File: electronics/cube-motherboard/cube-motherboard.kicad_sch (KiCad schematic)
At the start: 52 parts, among them J1 Conn_01x02, J2 Conn_02x04_Top_Bottom, J3 Conn_02x04_Top_Bottom, J4 Conn_02x04_Top_Bottom, J5 Conn_01x18, Q1 BSS138, Q2 BSS138, U1 Escon_24/2, U2 Escon_24/2, U3 Escon_24/2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

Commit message: Organize esp32 <-> escon wiring
Remapped AO1 of M3 to an ADC1 pin.
Removed all three unused AO2 DI3 wirings and relevant diodes and capacitors
Corrected pins.h (Old version was not matching with old schematic btw)
Updated Bom accordingly
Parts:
- removed C11, C7, C9: 0.1uF, Capacitor_SMD:C_0603_1608Metric, symbol Device:C
- removed D10, D6, D8: D_TVS, Diode_SMD:D_0402_1005Metric, symbol Device:D_TVS
- C11: renamed from C16; symbol Device:C_Polarized -> Device:C
- renumbered C15 to C10, C8 to C7, C10 to C8, C14 to C9, D7 to D6, D9 to D7
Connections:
- net AO1_M3: now also U4.7 (GPIO7/ADC1_CH6); no longer U4.8 (GPIO15/ADC2_CH4/32K_P)
- net AO2_M1: no longer names the net of U1.19 (AO2)
- net AO2_M1: no longer U4.17 (GPIO11/ADC2_CH0)
- net AO2_M2: no longer names the net of U4.12 (GPIO8/ADC1_CH7)
- net AO2_M2: no longer U2.19 (AO2)
- net AO2_M3: no longer names the net of U3.19 (AO2)
- net AO2_M3: no longer U4.7 (GPIO7/ADC1_CH6)
- net DI3_M1: no longer names the net of U1.15 (DIO3)
- net DI3_M1: no longer U4.20 (GPIO14/ADC2_CH3)
- net DI3_M2: no longer names the net of U4.9 (GPIO16/ADC2_CH5/32K_N)
- net DI3_M2: no longer U2.15 (DIO3)
- net DI3_M3: no longer names the net of U3.15 (DIO3)
- net DI3_M3: no longer U4.4 (GPIO4/ADC1_CH3)
- no-connect marks 46 -> 59
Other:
- moved on the sheet: C7, C8, D5, D6, D7

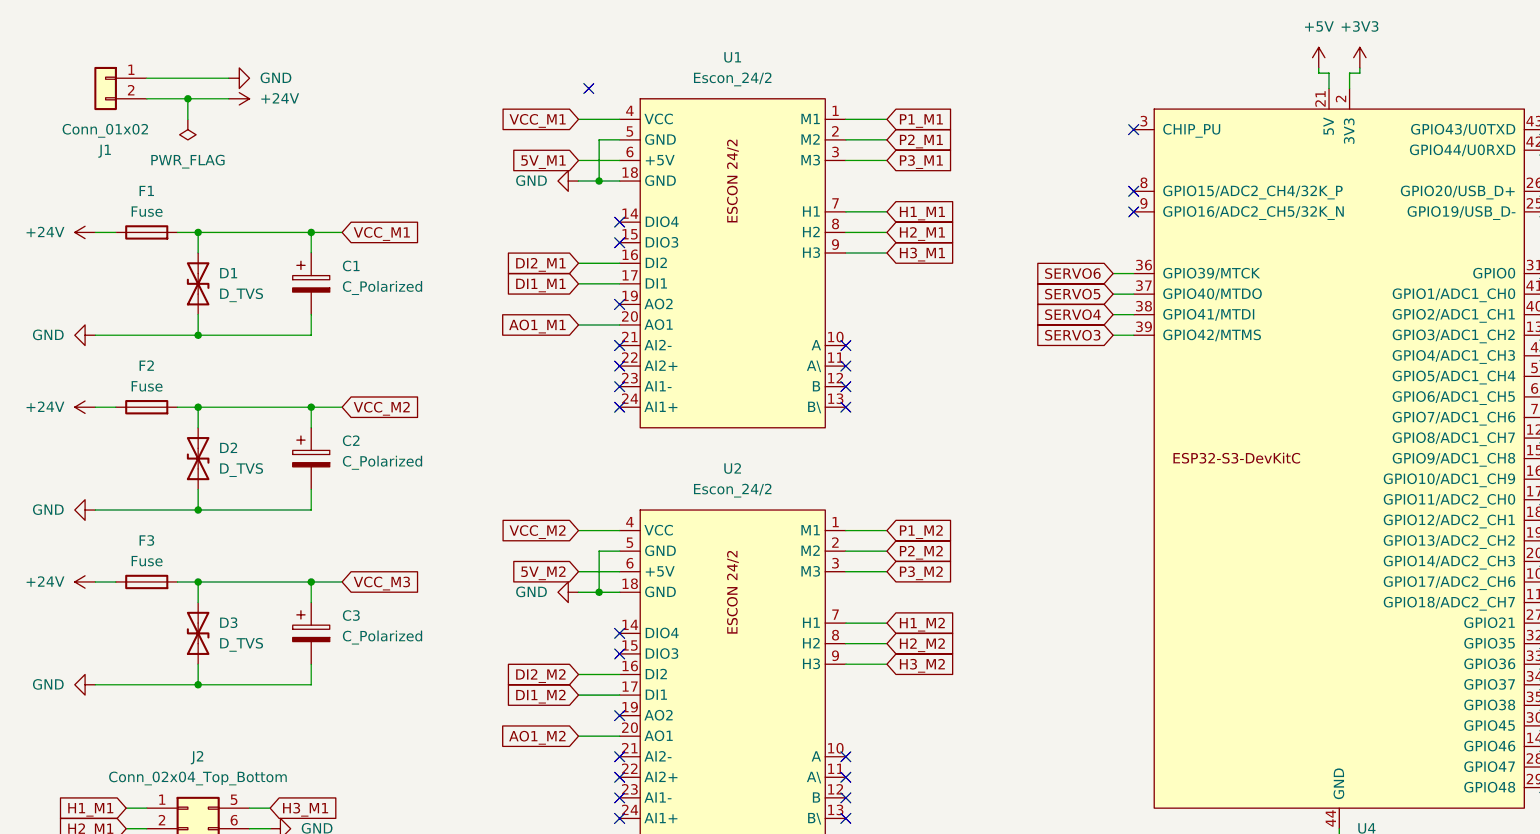
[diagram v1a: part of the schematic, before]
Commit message: Fix symbol, footprint and orientation of D1,D2 and D3 diodes
Add missing 3D models for L1 & F1,F2,F3
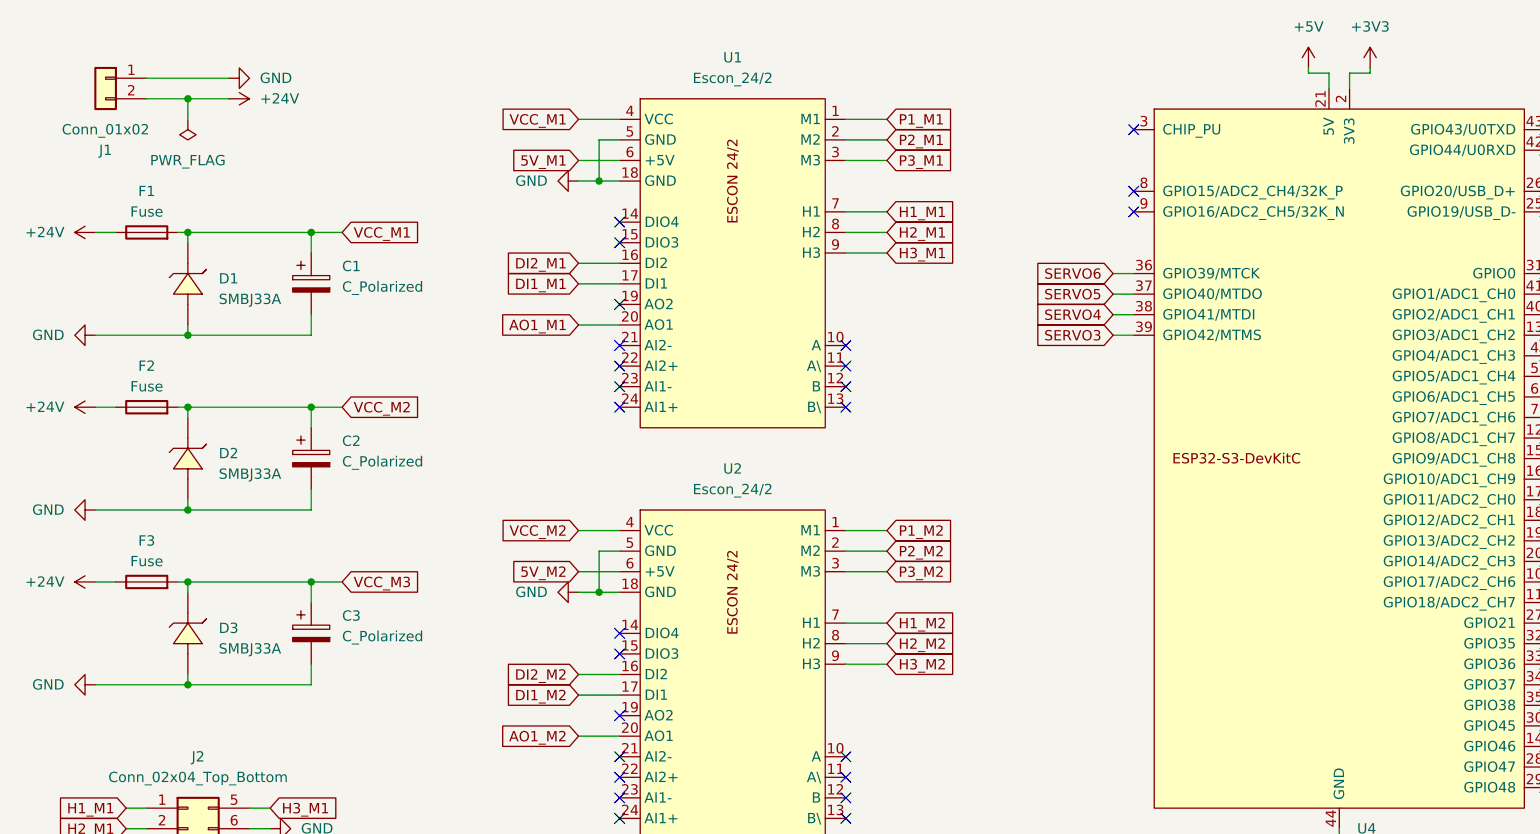
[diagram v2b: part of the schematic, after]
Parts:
- removed D1, D2, D3: D_TVS, Diode_SMD:D_SMB, symbol Device:D_TVS
- added D1, D2, D3: SMBJ33A, cube-motherboard:SMB_L4.4-W3.6-LS5.4-RD, symbol cube-motherboard:SMBJ33A
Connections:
- net GND: now also D1.2 (A), D2.2 (A), D3.2 (A)
- net VCC_M1: now also D1.1 (C)
- net VCC_M2: now also D2.1 (C)
- net VCC_M3: now also D3.1 (C)
- no-connect marks 59 -> 58

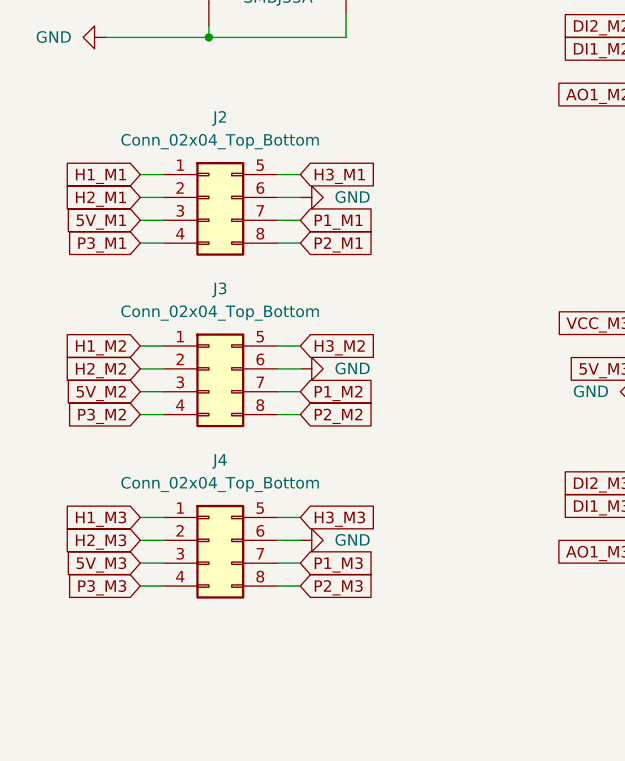
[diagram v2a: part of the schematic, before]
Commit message: Remove the requirement to remap the pins of the molex cables by reorganizing pin order
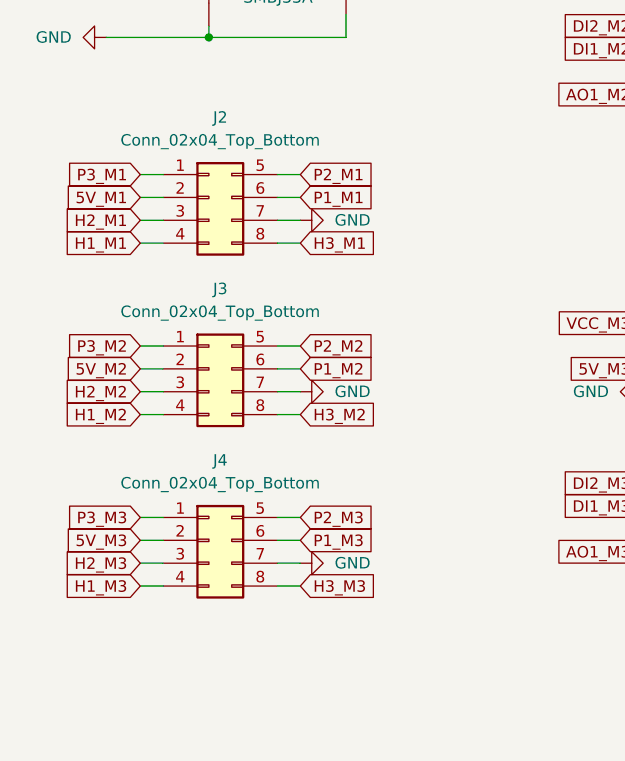
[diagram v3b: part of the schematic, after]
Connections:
- net 5V_M1: now also J2.2 (Pin_2); no longer J2.3 (Pin_3)
- net 5V_M2: now also J3.2 (Pin_2); no longer J3.3 (Pin_3)
- net 5V_M3: now also J4.2 (Pin_2); no longer J4.3 (Pin_3)
- net GND: now also J2.7 (Pin_7), J3.7 (Pin_7), J4.7 (Pin_7); no longer J2.6 (Pin_6), J3.6 (Pin_6), J4.6 (Pin_6)
- net H1_M1: now also J2.4 (Pin_4); no longer J2.1 (Pin_1)
- net H1_M2: now also J3.4 (Pin_4); no longer J3.1 (Pin_1)
- net H1_M3: now also J4.4 (Pin_4); no longer J4.1 (Pin_1)
- net H2_M1: now also J2.3 (Pin_3); no longer J2.2 (Pin_2)
- net H2_M2: now also J3.3 (Pin_3); no longer J3.2 (Pin_2)
- net H2_M3: now also J4.3 (Pin_3); no longer J4.2 (Pin_2)
- net H3_M1: now also J2.8 (Pin_8); no longer J2.5 (Pin_5)
- net H3_M2: now also J3.8 (Pin_8); no longer J3.5 (Pin_5)
- net H3_M3: now also J4.8 (Pin_8); no longer J4.5 (Pin_5)
- net P1_M1: now also J2.6 (Pin_6); no longer J2.7 (Pin_7)
- net P1_M2: now also J3.6 (Pin_6); no longer J3.7 (Pin_7)
- net P1_M3: now also J4.6 (Pin_6); no longer J4.7 (Pin_7)
- net P2_M1: now also J2.5 (Pin_5); no longer J2.8 (Pin_8)
- net P2_M2: now also J3.5 (Pin_5); no longer J3.8 (Pin_8)
- net P2_M3: now also J4.5 (Pin_5); no longer J4.8 (Pin_8)
- net P3_M1: now also J2.1 (Pin_1); no longer J2.4 (Pin_4)
- net P3_M2: now also J3.1 (Pin_1); no longer J3.4 (Pin_4)
- net P3_M3: now also J4.1 (Pin_1); no longer J4.4 (Pin_4)
